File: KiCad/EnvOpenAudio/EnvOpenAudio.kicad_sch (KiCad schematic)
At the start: 48 parts, among them J2 Button, J5 Conn_01x03_Male, U1 SOT-23-5 5.5V 3.3V 500mA, U3 RP2040, Y1 3225_4P 12MHz

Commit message: started work on RP2040 board
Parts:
- removed USB1: TYPE-C-31-M-12, HRO-TYPE-C31-M-12:HRO-TYPE-C-31-M-12, symbol Type-C:HRO-TYPE-C-31-M-12
- added J1: USB_C_Receptacle_USB2.0, Connector_USB:USB_C_Receptacle_HRO_TYPE-C-31-M-12, symbol Connector:USB_C_Receptacle_USB2.0
- J5: footprint Connector_PinHeader_2.54mm:PinHeader_1x03_P2.54mm_Vertical -> Connector_PinHeader_1.00mm:PinHeader_1x03_P1.00mm_Vertical
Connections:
- net GND: now also J1.A1 (GND), J1.A12 (GND), J1.B1 (GND), J1.B12 (GND)
- net USB_D+: now also J1.A6 (D+), J1.B6 (D+)
- net USB_D-: now also J1.A7 (D-), J1.B7 (D-)
- net VBUS: now also J1.A4 (VBUS), J1.A9 (VBUS), J1.B4 (VBUS), J1.B9 (VBUS)
- net at R6.2: now also J1.B5 (CC2)
- net at C101.2, R102.1: now also J1.S1 (SHIELD)
- net at R5.2: now also J1.A5 (CC1)
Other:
- moved on the sheet: C1, C101, C4, CBP1, D1, F1, FB1, NT1, R101, R102, R103, R5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

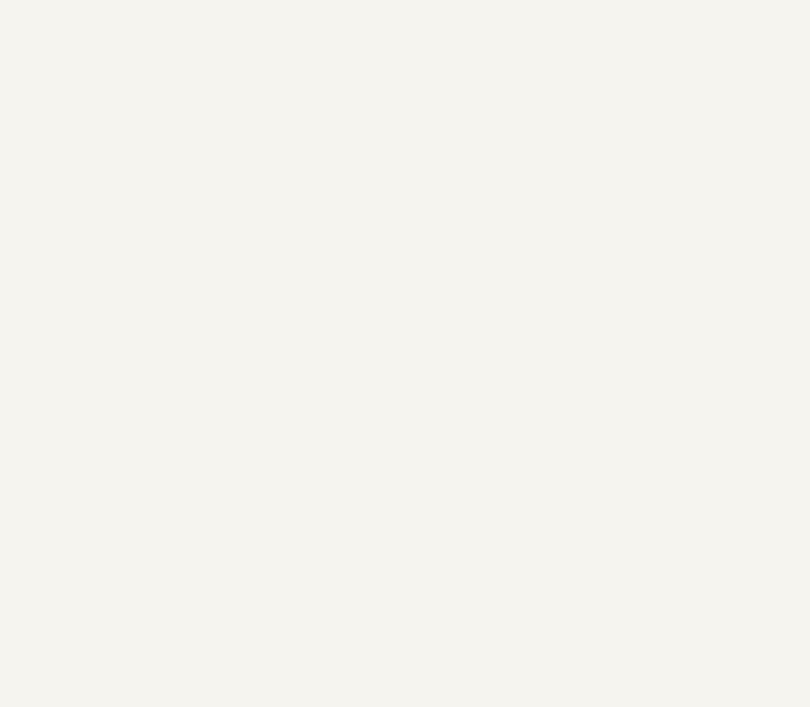
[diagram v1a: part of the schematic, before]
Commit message: added PCM3060, picked due to low cost.
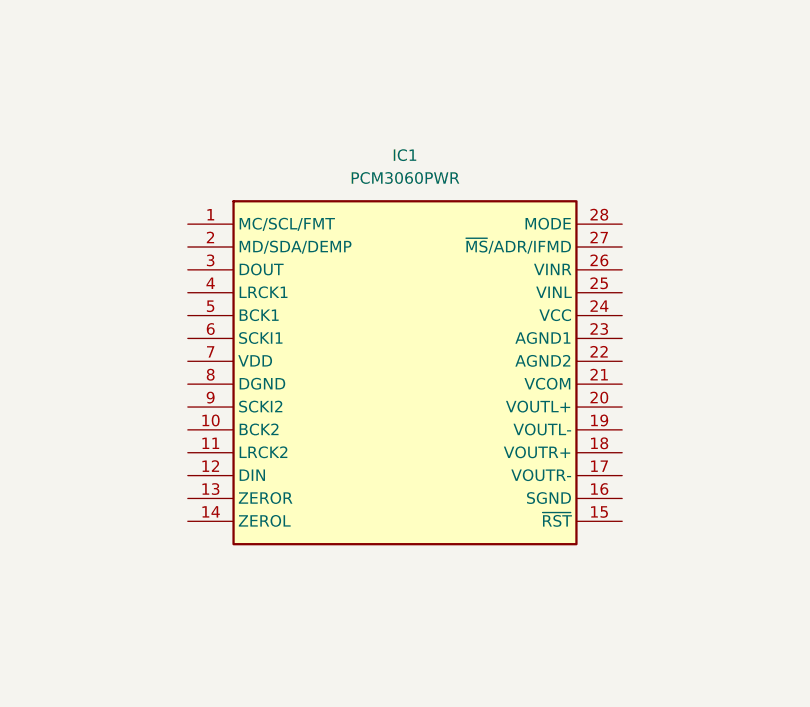
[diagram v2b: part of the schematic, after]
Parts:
- added IC1: PCM3060PWR, PCM3060PWR:SOP65P640X120-28N, symbol PCM3060PWR:PCM3060PWR
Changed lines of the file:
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@@
+    )
+  )
+  (symbol (lib_id "PCM3060PWR:PCM3060PWR") (at 259.715 36.83 0) (unit 1)
+    (in_bom yes) (on_board yes) (dnp no) (fields_autoplaced)
+    (property "Reference" "IC1" (at 283.845 29.21 0)
+      (effects (font (size 1.27 1.27)))
+    )
+    (property "Value" "PCM3060PWR" (at 283.845 31.75 0)
+      (effects (font (size 1.27 1.27)))
+    )
+    (property "Footprint" "PCM3060PWR:SOP65P640X120-28N" (at 304.165 131.75 0)
+      (effects (font (size 1.27 1.27)) (justify left top) hide)
+    )
+    (property "Datasheet" "https://www.ti.com/lit/ds/symlink/pcm3060.pdf?ts=1606824200789&ref_url=https%253A%252F%252Fwww.ti.com%252Fstore%252Fti%252Fen%252Fp%252Fproduct%252F%253Fp%253DPCM3060PWR%2526keyMatch%253DPCM3060PWR%2526tisearch%253DSearch-EN-everything%2526usecase%253DOPN" (at 304.165 231.75 0)
+      (effects (font (size 1.27 1.27)) (justify left top) hide)
+    )
+    (property "Height" "1.2" (at 304.165 431.75 0)
+      (effects (font (size 1.27 1.27)) (justify left top) hide)
+    )
+    (property "Mouser Part Number" "595-PCM3060PWR" (at 304.165 531.75 0)
+      (effects (font (size 1.27 1.27)) (justify left top) hide)
+    )
+    (property "Mouser Price/Stock" "https://www.mouser.co.uk/ProductDetail/Texas-Instruments/PCM3060PWR?qs=W5eanQMd1BA4oHiQoX9kuw%3D%3D" (at 304.165 631.75 0)
+      (effects (font (size 1.27 1.27)) (justify left top) hide)
+    )
+    (property "Manufacturer_Name" "Texas Instruments" (at 304.165 731.75 0)
+      (effects (font (size 1.27 1.27)) (justify left top) hide)
+    )
+    (property "Manufacturer_Part_Number" "PCM3060PWR" (at 304.165 831.75 0)
+      (effects (font (size 1.27 1.27)) (justify left top) hide)
+    )
+    (pin "1")
+    (pin "10")
+    (pin "11")
+    (pin "12")
+    (pin "13")
+    (pin "14")
+    (pin "15")
+    (pin "16")
+    (pin "17")
+    (pin "18")
+    (pin "19")
+    (pin "2")
+    (pin "20")
+    (pin "21")
+    (pin "22")
+    (pin "23")
+    (pin "24")
+    (pin "25")
+    (pin "26")
+    (pin "27")
+    (pin "28")
+    (pin "3")
+    (pin "4")
+    (pin "5")
+    (pin "6")
+    (pin "7")
+    (pin "8")
+    (pin "9")
+    (instances
+      (project "EnvOpenAudio"
+        (path "/7b892ee5-f34f-4bca-8f87-a56522432f7c"
+          (reference "IC1") (unit 1)
+        )
+      )
     )
   )

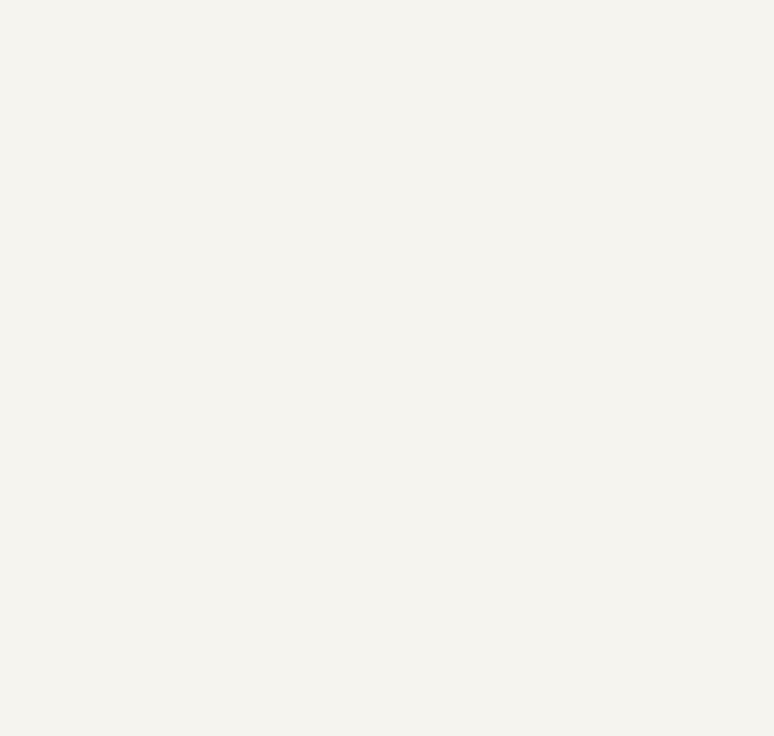
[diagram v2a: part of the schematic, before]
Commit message: added a couple notes on ANC and alternative IC.
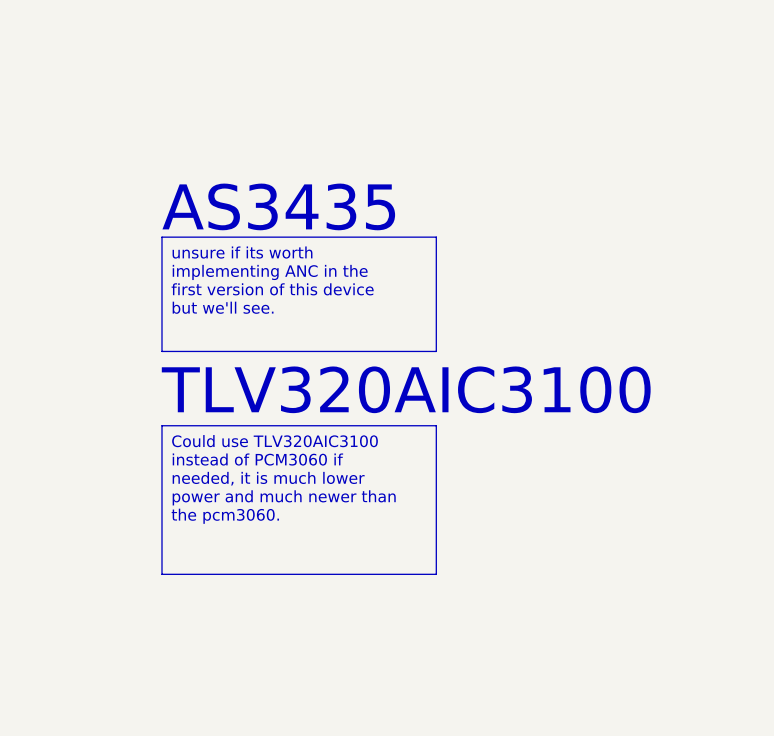
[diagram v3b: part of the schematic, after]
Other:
- note added: "AS3435"
- note added: "TLV320AIC3100"
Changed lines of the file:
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@@
     (stroke (width 0) (type default))
+  )
+  (text_box "Could use TLV320AIC3100  instead of PCM3060 if needed, it is much lower power and much newer than the pcm3060.\n"
+    (at 299.72 135.255 0) (size 30.48 16.51)
+    (stroke (width 0) (type default))
+    (fill (type none))
+    (effects (font (size 1.27 1.27)) (justify left top))
+  )
+  (text_box "unsure if its worth implementing ANC in the first version of this device but we'll see."
+    (at 299.72 114.3 0) (size 30.48 12.7)
+    (stroke (width 0) (type default))
+    (fill (type none))
+    (effects (font (size 1.27 1.27)) (justify left top))
   )
   (text "USB/POWER" (at 66.675 27.305 0)
@@
     (effects (font (size 1.27 1.27)) (justify left bottom))
   )
+  (text "AS3435 " (at 299.72 114.3 0)
+    (effects (font (size 5 5)) (justify left bottom))
+  )
   (text "Im unsure if the RP2040 can function with flash larger than 128Mb"
     (at 13.335 142.24 0)
@@
     (effects (font (size 1.27 1.27)) (justify left bottom))
   )
+  (text "TLV320AIC3100 " (at 299.72 134.62 0)
+    (effects (font (size 5 5)) (justify left bottom))
+  )
   (text "VBUS SENSE" (at 73.025 52.705 0)

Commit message: added some stuff, dont remember lol
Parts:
- added U2: LM3880, Package_TO_SOT_SMD:SOT-23-6, symbol Power_Supervisor:LM3880
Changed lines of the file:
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@@
+    (effects (font (size 1.27 1.27)) (justify left top))
+  )
+  (text_box "For the audio IC it says it needs power startup sqequence in the datasheet but im not sure how important this is."
+    (at 299.72 154.94 0) (size 30.48 32.385)
+    (stroke (width 0) (type default))
+    (fill (type none))
     (effects (font (size 1.27 1.27)) (justify left top))
   )
@@
         )
       )
+    )
+  )
+  (symbol (lib_id "Power_Supervisor:LM3880") (at 314.325 178.435 0) (unit 1)
+    (in_bom yes) (on_board yes) (dnp no) (fields_autoplaced)
+    (property "Reference" "U2" (at 316.5191 168.275 0)
+      (effects (font (size 1.27 1.27)) (justify left))
+    )
+    (property "Value" "LM3880" (at 316.5191 170.815 0)
+      (effects (font (size 1.27 1.27)) (justify left))
+    )
+    (property "Footprint" "Package_TO_SOT_SMD:SOT-23-6" (at 330.835 184.785 0)
+      (effects (font (size 1.27 1.27)) hide)
+    )
+    (property "Datasheet" "http://www.ti.com/lit/ds/symlink/lm3880.pdf" (at 314.325 178.435 0)
+      (effects (font (size 1.27 1.27)) hide)
+    )
+    (pin "6")
+    (pin "2")
+    (pin "1")
+    (pin "3")
+    (pin "5")
+    (pin "4")
+    (instances
+      (project "EnvOpenAudio"
+        (path "/7b892ee5-f34f-4bca-8f87-a56522432f7c"
+          (reference "U2") (unit 1)
+        )
+      )

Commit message: wired up audio IC
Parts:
- removed C102: 2.2uF 0402, Capacitor_SMD:C_0402_1005Metric, symbol Device:C
- removed CBP1: 10uf 0402, Capacitor_SMD:C_0402_1005Metric, symbol Device:C
- removed IC1: PCM3060PWR, PCM3060PWR:SOP65P640X120-28N, symbol PCM3060PWR:PCM3060PWR
- removed NT1: NetTie_2, NetTie:NetTie-2_SMD_Pad0.5mm, symbol Device:NetTie_2
- removed R10: 1 0402, Resistor_SMD:R_0402_1005Metric, symbol Device:R_Small
- removed R101: 5.6K 0402, Resistor_SMD:R_0402_1005Metric, symbol Device:R
- removed R103: 10K 0402, Resistor_SMD:R_0402_1005Metric, symbol Device:R
- removed R9: 200 0603, Resistor_SMD:R_0603_1608Metric, symbol Device:R_Small
- removed TP1, TP2, TP3: TestPoint, EnvExtras:CustomTestPoint, symbol Connector:TestPoint
- removed U1: SOT-23-5 5.5V 3.3V 500mA, Package_TO_SOT_SMD:SOT-23-5, symbol Regulator_Linear:AP131-15
- added C12, C20, C21, C9: 10uf 0402, Capacitor_SMD:C_0402_1005Metric, symbol Device:C_Small
- added C22, C24, C26, C28, C30, C32: 0.1mF 0402, Capacitor_SMD:C_0402_1005Metric, symbol Device:C_Small
- added C23, C25: 22mF 0402, Capacitor_SMD:C_0402_1005Metric, symbol Device:C_Small
- added C27, C29, C31, C33: 10mF 0402, Capacitor_SMD:C_0402_1005Metric, symbol Device:C_Small
- added C34, C35: 47mF 0402, Capacitor_SMD:C_0402_1005Metric, symbol Device:C_Small
- added C36, C37: 1mF 0402, Capacitor_SMD:C_0402_1005Metric, symbol Device:C_Small
- added R12, R8: 100K 0402, Resistor_SMD:R_0402_1005Metric, symbol Device:R_Small
- added R13: 22K 0402, Resistor_SMD:R_0402_1005Metric, symbol Device:R_Small
- added U1, U6: TLV75533PDBV, Package_TO_SOT_SMD:SOT-23-5, symbol Regulator_Linear:TLV75533PDBV
- added U4: TLV320AIC3100, Package_DFN_QFN:VQFN-32-1EP_5x5mm_P0.5mm_EP3.5x3.5mm, symbol Audio:TLV320AIC3100
- added U5: TLV75518PDBV, Package_TO_SOT_SMD:SOT-23-5, symbol Regulator_Linear:TLV75518PDBV
- D1: value 1N4002W -> schottky diode low forward voltage
- J2, RSW1: footprint Button_Switch_SMD:SW_Push_SPST_NO_Alps_SKRK -> Button_Switch_SMD:SW_SPST_B3U-1000P
- R7: symbol Device:R -> Device:R_Small
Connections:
- net +3V3: now also U3.43 (ADC_AVDD), C21.2, C28.1, C29.1, C30.1, C31.1, C32.1, C33.1, U1.5 (OUT), U4.17 (AVDD), U4.2 (IOVDD), U4.28 (HPVDD), U6.5 (OUT)
- net 3V3_EN: now also U1.3 (EN)
- net GND: now also C12.1, C20.1, C21.1, C22.2, C23.2, C24.2, C25.2, C26.2, C27.2, C28.2, C29.2, C30.2, C31.2, C32.2, C33.2, C9.1, U1.2 (GND), U4.1 (IOVSS), U4.16 (AVSS), U4.18 (DVSS), U4.20 (SPKVSS), U4.25 (SPKVSS), U4.29 (HPVSS), U4.33 (EP), U5.2 (GND), U6.2 (GND)
- net VSYS: now also C1.1, FB1.2, C20.2, C22.1, C23.1, C24.1, C25.1, C9.2, R12.2, R8.2, U1.1 (IN), U4.21 (SPKVDD), U4.24 (SPKVDD), U5.1 (IN), U6.1 (IN); no longer D1.1 (K), F1.2
- net GPIO0 renamed I2C0_SDA
- net I2C0_SDA: now also U4.9 (SDA)
- net GPIO1 renamed I2C0_SCL
- net I2C0_SCL: now also U4.10 (SCL)
- net GPIO2 renamed AUDIO_MCLK
- net AUDIO_MCLK: now also U4.8 (MCLK)
- net GPIO3 renamed AUDIO_BCLK
- net AUDIO_BCLK: now also U4.7 (BCLK)
- net GPIO4 renamed AUDIO_WCLK
- net AUDIO_WCLK: now also U4.6 (WCLK)
- net GPIO5 renamed AUDIO-DIN
- net AUDIO-DIN: now also U4.5 (DIN)
- net GPIO6 renamed AUDIO-DOUT
- net AUDIO-DOUT: now also U4.4 (DOUT)
- new net: D1.1 (K), F1.2
- new net: C34.1, U4.27 (HPL)
- new net: R12.1, U6.3 (EN)
- new net: C35.1, U4.30 (HPR)
- new net: R8.1, U5.3 (EN)
- new net: R13.2, U4.12 (MICBIAS)
- new net: C37.1, U4.13 (MIC1LP)
- new net: C36.1, U4.15 (MIC1LM)
- new net +1V8: C12.2, C26.1, C27.1, U4.3 (DVDD), U5.5 (OUT)
- new net HPLO: C34.2
- new net HPRO: C35.2
- new net MIC1LM: C36.2
- new net MIC1LP: C37.2
- new net MIC1RP: R13.1, U4.11 (VOL/MICDET), U4.14 (MIC1RP)
- new net SPKM: U4.19 (SPKM), U4.23 (SPKM)
- new net SPKP: U4.22 (SPKP), U4.26 (SPKP)
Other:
- note added: "SWAP FOR MORE POWERFUL 3V3 REGULATOR!"
- note removed: "1K resistor to prevent overdriving of the crystal as per the minimal design example"
- note removed: "2x 5.1K Resistors on the CC pins will = 5V@1.5A this is the recomended default config for type-c"
- note removed: "500mA hold current 1A trip 6V trip"
- note removed: "D1 NEEDS to be 0omh resistor or 1N4002 diode"
- note removed: "Flash"
- note removed: "GD25Q40CEIGR is NOT Compatible you need GD25W16* needs to be a multiple of 8 atleast for circuitpython. (Ive not confirmed if GD25W16 works I just Have some boards with GD25Q40CEIGR and they dont work)"
- note removed: "I think this is important for usb 3.0 but not 2.0 and 1.1 however it may help with analogue performance but ive yet to test this"
- note removed: "Im pretty sure a lot of these W25QXXX Chips are pin compatible Dont quote me on that"
- note removed: "Im unsure if the RP2040 can function with flash larger than 128Mb"
- note removed: "MAKE SURE THIS LINE is ran off of pin43 or close to pin43"
- note removed: "Make sure C3 is close to pin 45 of RP2040"
- note removed: "Make sure R3 and R4 are close to RP2040"
- note removed: "Make sure the flash chip you have selected supports 3.3V power or adjust the design."
- note removed: "Only fit cBP1 if you have selected an alternate voltage regulator TLV75533PDBVR does not require cBP1."
- note removed: "Pin 9 technically doesnt exist its the main central contact under the chip for heat dicipation"
- note removed: "RP2040 supports 1MHz to 15MHz"
- note removed: "Test points"
- note removed: "USB/POWER"
- note removed: "VBUS SENSE"
- note removed: "Would assume you could just not connect SD2 and SD3 for non QSPI"
- note removed: "https://datasheets.raspberrypi.com/rp2040/hardware-design-with-rp2040.pdf On page 13 you can learn more details of what flash is supported"
- note removed: "not 22pf but pick to match crystal."
- note removed: "suposedly the rp2040 supports SPI-2 flash but I havent tried it."
- note removed: "this is for factory testing always pull this to ground"
- moved on the sheet: C1, C10, C101, C11, C13, C14, C15, C16, C18, C3, C4, C5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
